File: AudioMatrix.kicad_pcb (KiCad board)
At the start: 2 copper layers, 100 x 100 mm, 112 parts, among them J1 AMP3, J2 AMP1, J3 AMP2, J4 Audio In, J5 3V3, J6 5V, J7 GND, J8 IO, J9 ESP, U1 PT2258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

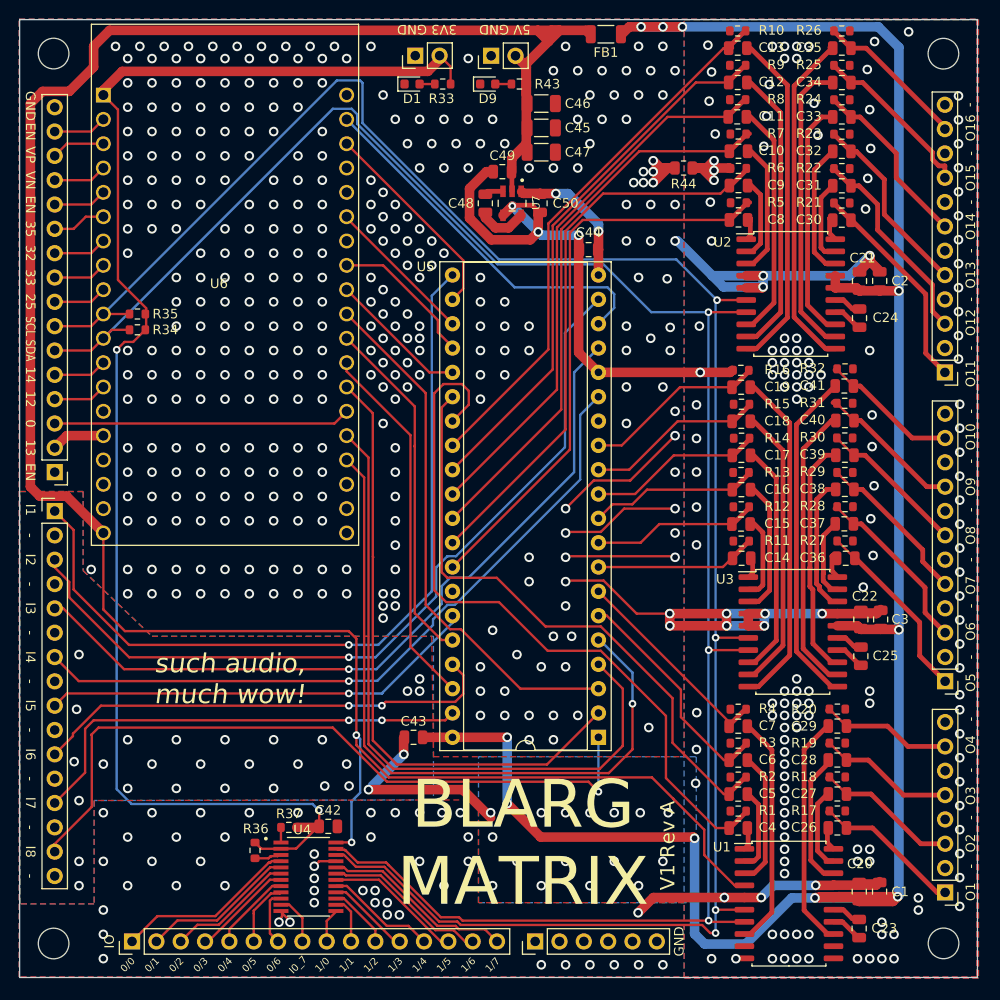
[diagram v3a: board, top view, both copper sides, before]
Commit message: pcb cosmetics
Step file for IO expander
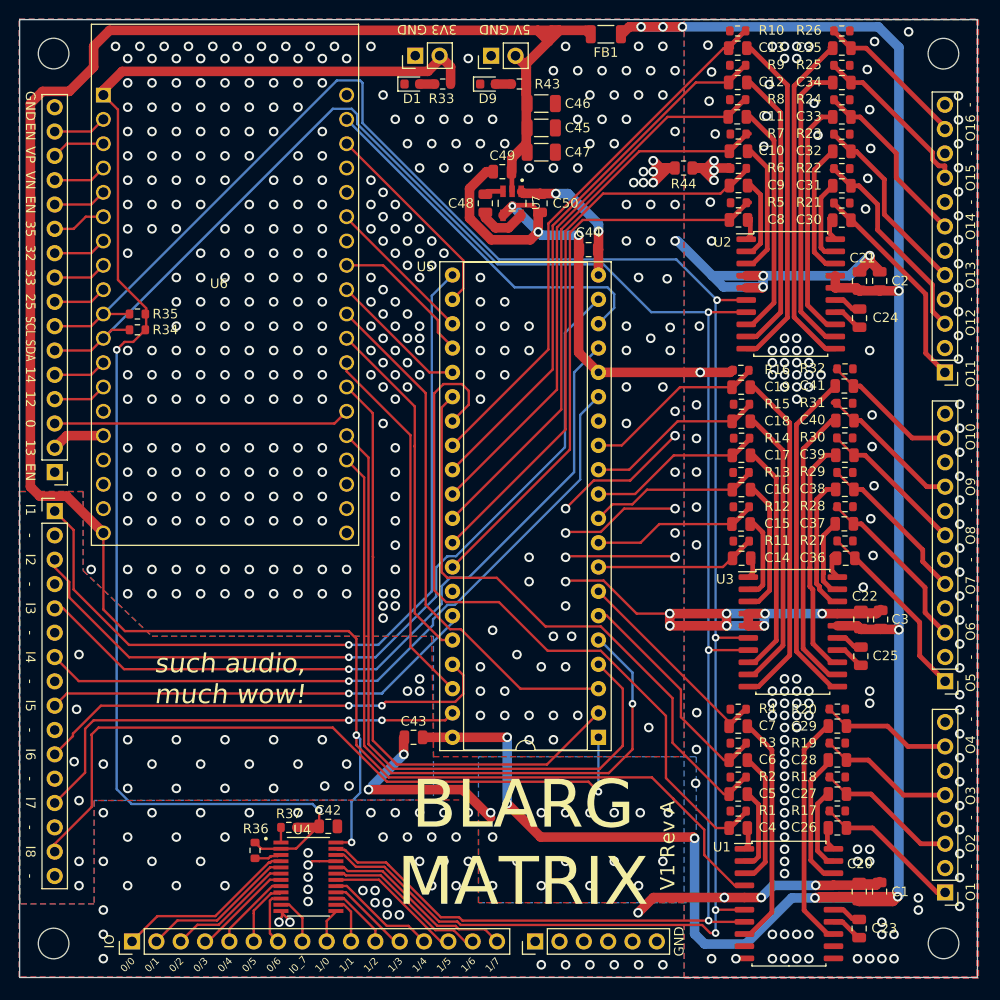
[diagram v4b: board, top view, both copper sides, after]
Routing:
- net GND: track 177.2 -> 177.8 mm, vias 393 -> 399
- net GNDA: vias 194 -> 196
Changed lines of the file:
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@@
     (thickness 1.6)
     (drawings 90)
-    (tracks 1570)
+    (tracks 1579)
     (zones 0)
     (modules 112)
@@
   )
   (setup
-    (last_trace_width 0.25)
+    (last_trace_width 1)
     (user_trace_width 0.25)
     (user_trace_width 0.5)
@@
     (pad 1 smd rect (at -2.87 -3.575) (size 1.57 0.41) (layers F.Cu F.Paste F.Mask)
       (net 142 "Net-(R37-Pad1)"))
+    (model ${KIPRJMOD}/components/TPS60403DBVR/SOT95P280X145-5N.kicad_mod
+      (at (xyz 0 0 0))
+      (scale (xyz 1 1 1))
+      (rotate (xyz 0 0 0))
+    )
+    (model ${KIPRJMOD}/components/TCA6416APWR/TCA6416APWR.step
+      (at (xyz 0 0 0))
+      (scale (xyz 1 1 1))
+      (rotate (xyz -90 0 90))
+    )
   )
   (module Resistor_SMD:R_0603_1608Metric (layer F.Cu)
@@
   (via (at 179.9111 83.31836) (size 1) (drill 0.6) (layers F.Cu B.Cu) (net 2))
   (via (at 188.8011 84.58836) (size 1) (drill 0.6) (layers F.Cu B.Cu) (net 2))
+  (via (at 179.909 118.872) (size 1) (drill 0.6) (layers F.Cu B.Cu) (net 2))
+  (via (at 178.639 120.142) (size 1) (drill 0.6) (layers F.Cu B.Cu) (net 2))
   (segment (start 132.9211 92.20836) (end 134.1911 90.93836) (width 0.25) (layer F.Cu) (net 3))
   (segment (start 103.7111 92.20836) (end 132.9211 92.20836) (width 0.25) (layer F.Cu) (net 3))
@@
   (via (at 141.8111 74.42836) (size 1) (drill 0.6) (layers F.Cu B.Cu) (net 14))
   (via (at 143.0811 75.69836) (size 1) (drill 0.6) (layers F.Cu B.Cu) (net 14))
-  (via (at 144.145 132.84836) (size 1) (drill 0.6) (layers F.Cu B.Cu) (net 14))
-  (via (at 146.05 132.84836) (size 1) (drill 0.6) (layers F.Cu B.Cu) (net 14))
+  (via (at 144.349 132.84836) (size 1) (drill 0.6) (layers F.Cu B.Cu) (net 14))
+  (via (at 146.889 132.842) (size 1) (drill 0.6) (layers F.Cu B.Cu) (net 14))
   (via (at 111.3311 54.10836) (size 1) (drill 0.6) (layers F.Cu B.Cu) (net 14))
   (via (at 113.8711 54.10836) (size 1) (drill 0.6) (layers F.Cu B.Cu) (net 14))
@@
   (via (at 138.43 143.51) (size 1) (drill 0.6) (layers F.Cu B.Cu) (net 14))
   (via (at 139.7 143.51) (size 1) (drill 0.6) (layers F.Cu B.Cu) (net 14))
-  (via (at 130.81 137.16) (size 1) (drill 0.6) (layers F.Cu B.Cu) (net 14))
-  (via (at 130.81 138.43) (size 1) (drill 0.6) (layers F.Cu B.Cu) (net 14))
-  (via (at 130.81 139.7) (size 1) (drill 0.6) (layers F.Cu B.Cu) (net 14))
-  (via (at 130.81 140.97) (size 1) (drill 0.6) (layers F.Cu B.Cu) (net 14))
-  (via (at 130.81 142.24) (size 1) (drill 0.6) (layers F.Cu B.Cu) (net 14))
+  (via (at 130.1623 137.033) (size 1) (drill 0.6) (layers F.Cu B.Cu) (net 14))
+  (via (at 130.1623 138.303) (size 1) (drill 0.6) (layers F.Cu B.Cu) (net 14))
+  (via (at 130.1623 139.573) (size 1) (drill 0.6) (layers F.Cu B.Cu) (net 14))
+  (via (at 130.1623 140.843) (size 1) (drill 0.6) (layers F.Cu B.Cu) (net 14))
+  (via (at 130.1623 142.113) (size 1) (drill 0.6) (layers F.Cu B.Cu) (net 14))
   (via (at 127.127 144.272) (size 1) (drill 0.6) (layers F.Cu B.Cu) (net 14))
   (via (at 128.27 144.272) (size 1) (drill 0.6) (layers F.Cu B.Cu) (net 14))
@@
   (via (at 139.269 132.842) (size 1) (drill 0.6) (layers F.Cu B.Cu) (net 14))
   (via (at 136.729 132.842) (size 1) (drill 0.6) (layers F.Cu B.Cu) (net 14))
-  (via (at 136.729 135.382) (size 1) (drill 0.6) (layers F.Cu B.Cu) (net 14))
   (via (at 141.809 137.922) (size 1) (drill 0.6) (layers F.Cu B.Cu) (net 14))
-  (via (at 144.349 140.462) (size 1) (drill 0.6) (layers F.Cu B.Cu) (net 14))
-  (via (at 146.889 135.382) (size 1) (drill 0.6) (layers F.Cu B.Cu) (net 14))
   (via (at 146.889 137.922) (size 1) (drill 0.6) (layers F.Cu B.Cu) (net 14))
   (via (at 157.684 114.427) (size 1) (drill 0.6) (layers F.Cu B.Cu) (net 14))
@@
   (segment (start 133.35 134.23166) (end 133.3109 134.27076) (width 0.25) (layer F.Cu) (net 14) (status 30))
   (segment (start 131.3301 137.9099) (end 133.0712 137.9099) (width 0.25) (layer F.Cu) (net 14))
-  (segment (start 130.81 138.43) (end 131.3301 137.9099) (width 0.25) (layer F.Cu) (net 14))
   (segment (start 172.3673 76.77786) (end 168.7097 73.12026) (width 1) (layer B.Cu) (net 14))
   (via (at 168.479 73.152) (size 1) (drill 0.6) (layers F.Cu B.Cu) (net 14))
@@
   (segment (start 177.66955 77.95261) (end 177.5743 78.04786) (width 1) (layer F.Cu) (net 14))
   (via (at 177.66955 77.95261) (size 1) (drill 0.6) (layers F.Cu B.Cu) (net 14))
+  (segment (start 130.5554 137.9099) (end 131.3301 137.9099) (width 0.25) (layer F.Cu) (net 14))
+  (segment (start 130.1623 138.303) (end 130.5554 137.9099) (width 0.25) (layer F.Cu) (net 14))
+  (via (at 168.479 61.722) (size 1) (drill 0.6) (layers F.Cu B.Cu) (net 14))
+  (via (at 162.129 62.992) (size 1) (drill 0.6) (layers F.Cu B.Cu) (net 14))
+  (via (at 143.079 135.382) (size 1) (drill 0.6) (layers F.Cu B.Cu) (net 14))
+  (via (at 140.539 135.382) (size 1) (drill 0.6) (layers F.Cu B.Cu) (net 14))
+  (via (at 144.349 137.922) (size 1) (drill 0.6) (layers F.Cu B.Cu) (net 14))
+  (via (at 145.619 135.382) (size 1) (drill 0.6) (layers F.Cu B.Cu) (net 14))
+  (via (at 145.619 140.462) (size 1) (drill 0.6) (layers F.Cu B.Cu) (net 14))
+  (via (at 143.079 140.462) (size 1) (drill 0.6) (layers F.Cu B.Cu) (net 14))
+  (via (at 137.999 135.382) (size 1) (drill 0.6) (layers F.Cu B.Cu) (net 14))
   (segment (start 191.8452 78.36146) (end 191.8452 113.75146) (width 1) (layer B.Cu) (net 16))
   (via (at 191.8452 78.36146) (size 1) (drill 0.6) (layers F.Cu B.Cu) (net 16))
@@
   (segment (start 196.6497 61.47436) (end 196.6497 61.24576) (width 0.5) (layer F.Cu) (net 69) (status 30))
   (segment (start 188.425872 53.021932) (end 186.9303 53.021932) (width 0.5) (layer F.Cu) (net 69) (status 20))
-  (segment (start 145.047 54.95666) (end 143.8939 53.80356) (width 0.25) (layer F.Cu) (net 140) (status 20))
-  (segment (start 145.047 56.769) (end 145.047 54.95666) (width 0.25) (layer F.Cu) (net 140) (status 10))
   (segment (start 113.1721 82.42936) (end 111.90846 83.693) (width 0.25) (layer F.Cu) (net 140))
   (segment (start 111.90846 83.693) (end 111.00546 83.693) (width 0.25) (layer F.Cu) (net 140))
@@
   (segment (start 120.4751 143.64336) (end 126.064449 138.054011) (width 0.25) (layer F.Cu) (net 98))
   (segment (start 114.4299 143.64336) (end 120.4751 143.64336) (width 0.25) (layer F.Cu) (net 98))
-  (segment (start 143.397 56.769) (end 141.809 56.769) (width 0.25) (layer F.Cu) (net 99) (status 30))
-  (segment (start 151.398 56.769) (end 149.7085 56.769) (width 0.25) (layer F.Cu) (net 100) (status 30))
   (segment (start 175.9849 134.32356) (end 176.1099 134.44856) (width 0.5) (layer F.Cu) (net 101) (status 30))
   (segment (start 176.1099 134.44856) (end 176.1099 134.67926) (width 0.5) (layer F.Cu) (net 101) (status 30))
@@
   (segment (start 126.406198 141.8099) (end 126.178301 142.037797) (width 0.25) (layer F.Cu) (net 92))
   (segment (start 127.3312 141.8099) (end 126.406198 141.8099) (width 0.25) (layer F.Cu) (net 92))
+  (segment (start 141.809 56.769) (end 143.397 56.769) (width 1) (layer F.Cu) (net 99))
+  (segment (start 149.7085 56.769) (end 151.398 56.769) (width 1) (layer F.Cu) (net 100))
   (segment (start 184.600342 132.663302) (end 186.3729 134.43586) (width 0.25) (layer F.Cu) (net 108))
   (segment (start 184.5979 132.663302) (end 184.600342 132.663302) (width 0.25) (layer F.Cu) (net 108))
@@
   (segment (start 131.21546 134.3787) (end 131.3234 134.27076) (width 1) (layer F.Cu) (net 140))
   (segment (start 128.9815 134.3787) (end 131.21546 134.3787) (width 1) (layer F.Cu) (net 140))
+  (segment (start 145.047 54.95666) (end 143.8939 53.80356) (width 1) (layer F.Cu) (net 140))
+  (segment (start 145.047 56.769) (end 145.047 54.95666) (width 1) (layer F.Cu) (net 140))
   (segment (start 126.99239 137.379899) (end 126.99239 137.2599) (width 0.25) (layer F.Cu) (net 141))
   (segment (start 126.286199 137.379899) (end 126.99239 137.379899) (width 0.25) (layer F.Cu) (net 141))

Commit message: Changed component placement of volume controllers
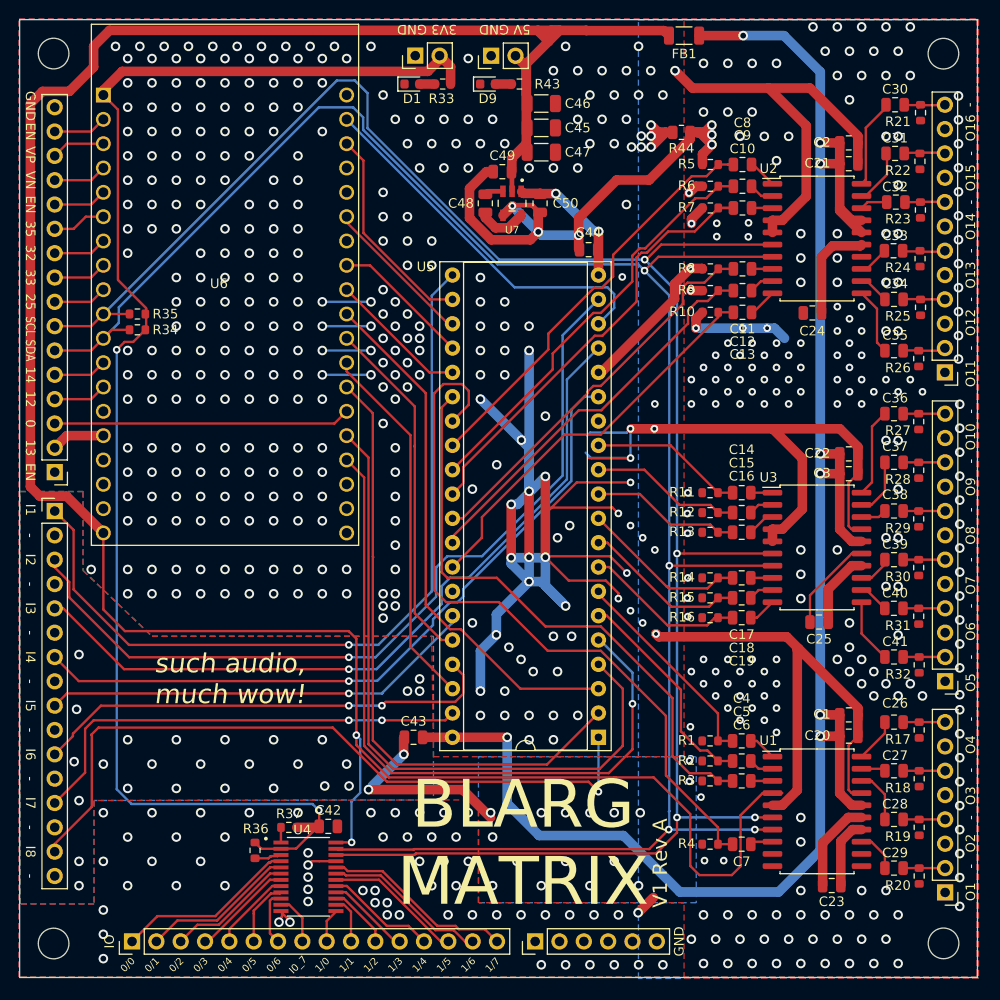
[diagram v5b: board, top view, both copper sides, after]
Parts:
- moved R26 35.1 mm to (193.9, 85.4), turned to 270 degrees
- moved C35 32.1 mm to (191.3, 84.6)
- moved R32 31.9 mm to (194.0, 117.4), turned to 270 degrees
- moved R10 29.5 mm to (172.2, 80.6)
- moved C41 28.8 mm to (191.3, 116.6)
- moved C13 27.6 mm to (175.5, 80.6)
- moved R25 26.6 mm to (194.1, 80.1), turned to 270 degrees
- moved R16 26.0 mm to (172.1, 112.5)
- moved C19 24.1 mm to (175.4, 112.5)
- moved R9 23.7 mm to (172.2, 78.3)
- moved R31 23.5 mm to (193.9, 112.3), turned to 270 degrees
- moved C34 23.3 mm to (191.3, 79.3)
- moved C12 21.7 mm to (175.5, 78.3)
- moved R15 20.5 mm to (172.1, 110.4)
- moved C40 20.3 mm to (191.3, 111.5)
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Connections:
- C10 pad 2: /IN13 -> /IN14
- C11 pad 2: /IN14 -> /IN13
- C12 pad 2: /IN15 -> /IN12
- C13 pad 2: /IN16 -> /IN11
- C14 pad 2: /IN5 -> /IN10
- C15 pad 2: /IN6 -> /IN9
- C16 pad 2: /IN7 -> /IN8
- C17 pad 2: /IN8 -> /IN7
- C18 pad 2: /IN9 -> /IN6
- C19 pad 2: /IN10 -> /IN5
- C4 pad 2: /IN1 -> /IN4
- C5 pad 2: /IN2 -> /IN3
- C6 pad 2: /IN3 -> /IN2
- C7 pad 2: /IN4 -> /IN1
- C8 pad 2: /IN11 -> /IN16
- C9 pad 2: /IN12 -> /IN15
- J1 pad 1: Net-(C26-Pad1) -> GNDA
- J1 pad 2: GNDA -> Net-(C29-Pad1)
- J1 pad 3: Net-(C27-Pad1) -> GNDA
- J1 pad 4: GNDA -> Net-(C28-Pad1)
- J1 pad 5: Net-(C28-Pad1) -> GNDA
- J1 pad 6: GNDA -> Net-(C27-Pad1)
- J1 pad 7: Net-(C29-Pad1) -> GNDA
- J1 pad 8: GNDA -> Net-(C26-Pad1)
- J2 pad 1: Net-(C30-Pad1) -> GNDA
- J2 pad 10: GNDA -> Net-(C31-Pad1)
- J2 pad 11: Net-(C35-Pad1) -> GNDA
- J2 pad 12: GNDA -> Net-(C30-Pad1)
- J2 pad 2: GNDA -> Net-(C35-Pad1)
- J2 pad 3: Net-(C31-Pad1) -> GNDA
- J2 pad 4: GNDA -> Net-(C34-Pad1)
- J2 pad 5: Net-(C32-Pad1) -> GNDA
- J2 pad 6: GNDA -> Net-(C33-Pad1)
- J2 pad 7: Net-(C33-Pad1) -> GNDA
- J2 pad 8: GNDA -> Net-(C32-Pad1)
- J2 pad 9: Net-(C34-Pad1) -> GNDA
- J3 pad 1: Net-(C36-Pad1) -> GNDA
- J3 pad 10: GNDA -> Net-(C37-Pad1)
- J3 pad 11: Net-(C41-Pad1) -> GNDA
- J3 pad 12: GNDA -> Net-(C36-Pad1)
- J3 pad 2: GNDA -> Net-(C41-Pad1)
- J3 pad 3: Net-(C37-Pad1) -> GNDA
- J3 pad 4: GNDA -> Net-(C40-Pad1)
- J3 pad 5: Net-(C38-Pad1) -> GNDA
- J3 pad 6: GNDA -> Net-(C39-Pad1)
- J3 pad 7: Net-(C39-Pad1) -> GNDA
- J3 pad 8: GNDA -> Net-(C38-Pad1)
- J3 pad 9: Net-(C40-Pad1) -> GNDA
- R1 pad 1: /IN1 -> /IN4
- R10 pad 1: /IN16 -> /IN11
- R11 pad 1: /IN5 -> /IN10
- R12 pad 1: /IN6 -> /IN9
- R13 pad 1: /IN7 -> /IN8
- R14 pad 1: /IN8 -> /IN7
- R15 pad 1: /IN9 -> /IN6
- R16 pad 1: /IN10 -> /IN5
- R2 pad 1: /IN2 -> /IN3
- R3 pad 1: /IN3 -> /IN2
- R4 pad 1: /IN4 -> /IN1
- R5 pad 1: /IN11 -> /IN16
- R6 pad 1: /IN12 -> /IN15
- R7 pad 1: /IN13 -> /IN14
- R8 pad 1: /IN14 -> /IN13
- R9 pad 1: /IN15 -> /IN12
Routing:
- net GND: track 177.8 -> 320.3 mm, vias 399 -> 376
- net +5VA: track 237.4 -> 196.4 mm, vias 10 -> 8
- net Net-(C19-Pad1): track 35.4 -> 2.93 mm
- net Net-(C13-Pad1): track 35.4 -> 3.01 mm
- net Net-(C35-Pad2): track 35.6 -> 6.98 mm
- net Net-(C41-Pad2): track 35.2 -> 6.73 mm
- net GNDA: track 98.1 -> 126.5 mm, vias 196 -> 269
- net Net-(C34-Pad2): track 31.4 -> 3.22 mm
- net Net-(C12-Pad1): track 30.0 -> 2.59 mm
- net Net-(C18-Pad1): track 29.7 -> 2.60 mm
- net Net-(C40-Pad2): track 30.2 -> 3.22 mm
- net Net-(C11-Pad1): track 24.4 -> 2.19 mm
- net Net-(C33-Pad2): track 25.4 -> 3.15 mm
- net Net-(C7-Pad1): track 24.4 -> 2.26 mm
- net Net-(C17-Pad1): track 24.4 -> 2.26 mm
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
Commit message: Net labeling and cleanup
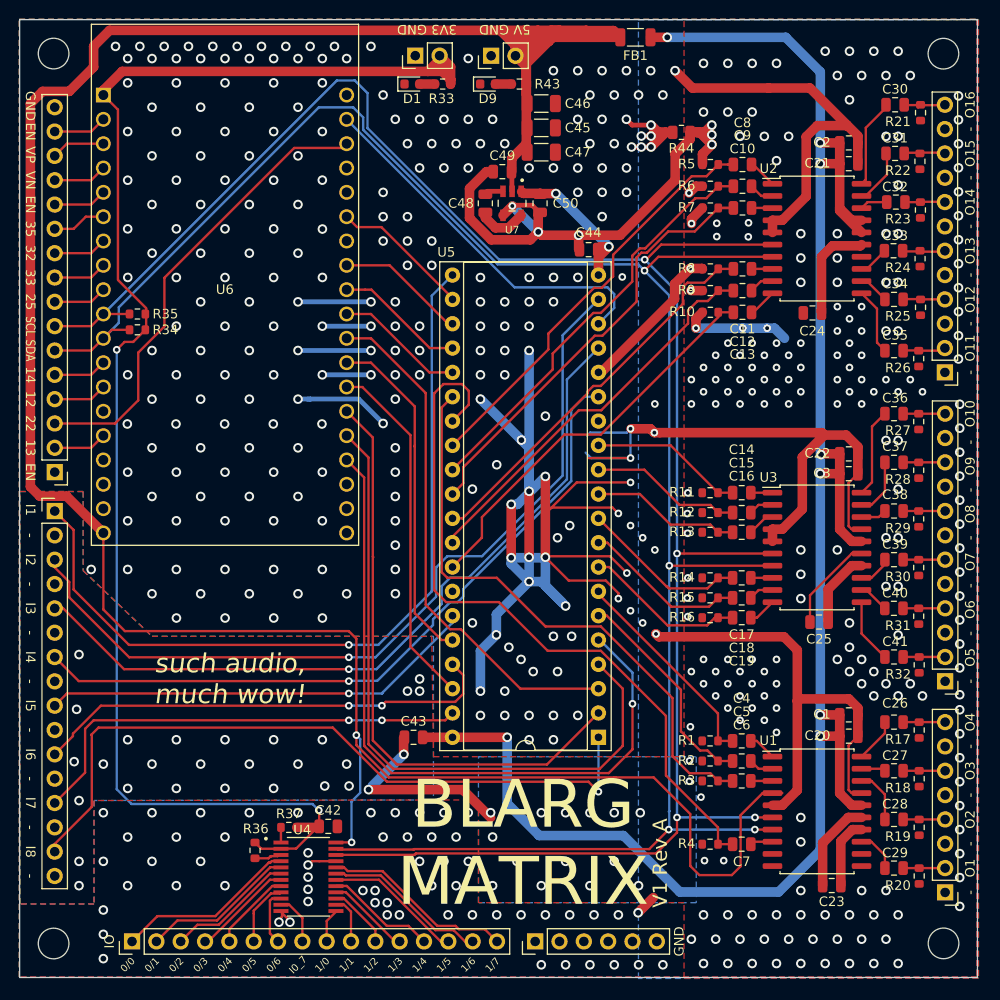
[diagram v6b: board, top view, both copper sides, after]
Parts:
- moved FB1 5.08 mm to (164.3, 51.9)
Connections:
- net /IN1 renamed /X12
- net /IN10 renamed /X11
- net /IN11 renamed /X0
- net /IN12 renamed /X1
- net /IN13 renamed /X2
- net /IN14 renamed /X3
- net /IN15 renamed /X4
- net /IN16 renamed /X5
- net /IN2 renamed /X13
- net /IN3 renamed /X14
- net /IN4 renamed /X15
- net /IN5 renamed /X6
- net /IN6 renamed /X7
- net /IN7 renamed /X8
- net /IN8 renamed /X9
- net /IN9 renamed /X10
- J9 pad 3: /GPIO0 -> /GPIO22
- U6 pad 22: /AX1 -> /GPIO22
- U6 pad 25: /AX2 -> /AX1
- U6 pad 27: /AY0 -> /AX2
- U6 pad 28: /AY1 -> /AY0
- U6 pad 29: /RESET -> /AY1
- U6 pad 30: /CS -> /RESET
- U6 pad 31: /DATA -> /CS
- U6 pad 32: /AY2 -> /DATA
- U6 pad 33: /GPIO0 -> /AY2
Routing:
- net /GPIO22: track 0.00 -> 48.5 mm
- net /GPIO0: track 31.0 -> 0.00 mm
- net +5V: track 267.9 -> 289.1 mm
- net GND: track 320.3 -> 341.4 mm, vias 376 -> 312
- net /AX1: track 22.2 -> 14.7 mm
- net +3V3: track 150.7 -> 156.9 mm
- net +5VA: track 196.4 -> 201.3 mm
- net /AY2: track 64.8 -> 62.3 mm
- net /AX2: track 16.0 -> 13.6 mm
- net -5VA: track 14.3 -> 16.2 mm
- net /DATA: track 38.6 -> 37.0 mm
- net /AY0: track 14.6 -> 13.6 mm
- net /AY1: track 14.6 -> 13.6 mm
- net /CS: track 36.9 -> 35.8 mm
- net /RESET: track 55.4 -> 54.4 mm
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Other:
- board text added: "22"
- board text removed: "0"
